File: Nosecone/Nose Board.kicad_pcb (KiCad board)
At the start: 2 copper layers, 45.7 x 63.5 mm, 48 parts, among them J1 Conn_01x02, J2 Conn_02x04_Odd_Even, J3 Conn_02x03_Odd_Even, J4 Conn_Coaxial, J5 Conn_01x02, Q1 Q_PMOS_DGS, Q2 Q_PMOS_DGS, U1 RS485_converter_ISL83488, U10 MS5803-14BA, U11 MS5803-14BA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

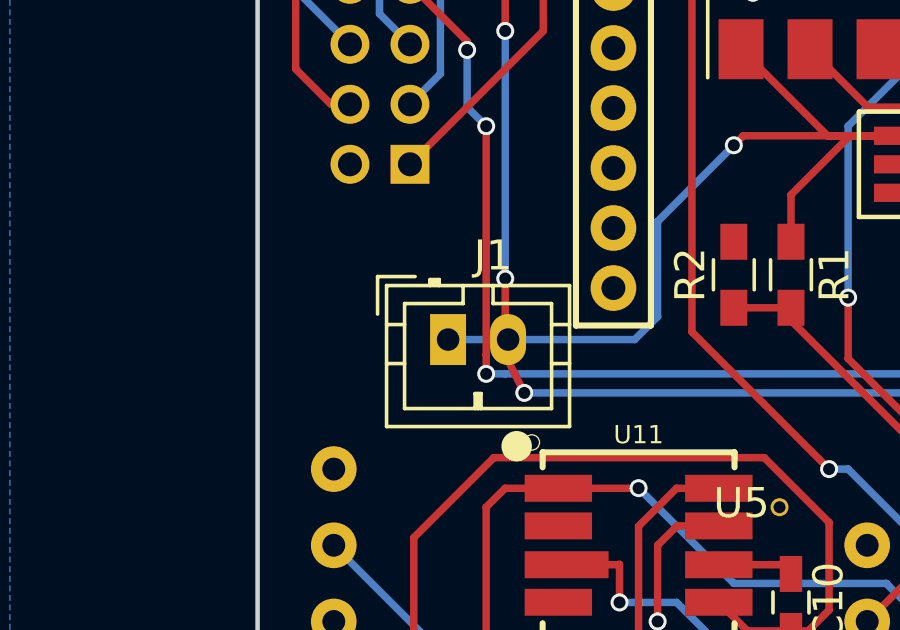
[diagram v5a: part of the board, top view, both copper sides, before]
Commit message: Layout/BoM adjustments
Known annular ring size problems, will fix those soon-ish
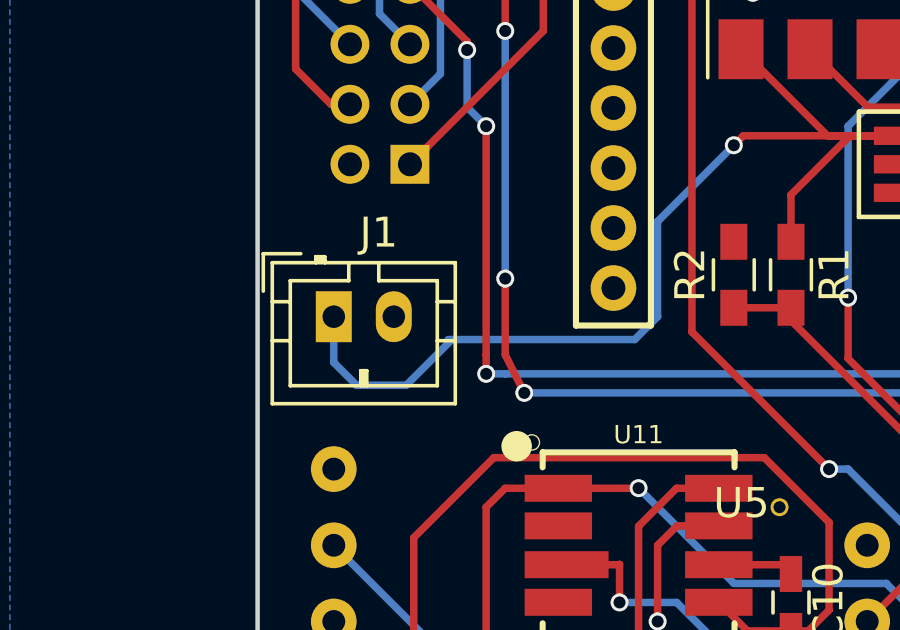
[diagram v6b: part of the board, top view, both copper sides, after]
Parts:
- moved J1 3.89 mm to (137.2, 83.8)
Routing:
- net GND: track 46.0 -> 5.07 mm, vias 4 -> 0
- net /Debug_RX: track 4.05 -> 45.0 mm, vias 1 -> 5
- net +BATT: track 31.9 -> 38.3 mm
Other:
- net class Default: via_drill 0.4 -> 0.3
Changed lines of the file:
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@@
   (general
     (links 149)
-    (no_connects 58)
-    (area 134.544999 55.804999 180.415001 119.455001)
+    (no_connects 57)
+    (area 124.46 43.18 195.580001 142.240001)
     (thickness 1.6)
-    (drawings 10)
-    (tracks 479)
+    (drawings 8)
+    (tracks 484)
     (zones 0)
     (modules 48)
@@
     (edge_width 0.15)
     (via_size 0.6)
-    (via_drill 0.4)
+    (via_drill 0.3)
     (via_min_size 0.4)
     (via_min_drill 0.3)
@@
     (visible_elements 7FFEFFFF)
     (pcbplotparams
-      (layerselection 0x00030_80000001)
+      (layerselection 0x010f0_80000001)
       (usegerberextensions false)
       (excludeedgelayer true)
       (linewidth 0.100000)
       (plotframeref false)
-      (viasonmask false)
+      (viasonmask true)
       (mode 1)
       (useauxorigin false)
@@
       (padsonsilk false)
       (subtractmaskfromsilk false)
-      (outputformat 1)
+      (outputformat 4)
       (mirror false)
-      (drillshape 1)
+      (drillshape 2)
       (scaleselection 1)
-      (outputdirectory ""))
+      (outputdirectory PDFs/))
   )
   (net 0 "")
@@
     (trace_width 0.25)
     (via_dia 0.6)
-    (via_drill 0.4)
+    (via_drill 0.3)
     (uvia_dia 0.3)
     (uvia_drill 0.1)
@@
   )
   (module Connectors_JST:JST_PH_B2B-PH-K_02x2.00mm_Straight (layer F.Cu)
-    (at 140.97 84.582)
+    (at 137.16 83.82)
     (descr "JST PH series connector, B2B-PH-K, top entry type, through hole, Datasheet: http://www.jst-mfg.com/product/pdf/eng/ePH.pdf")
     (tags "connector jst ph")
@@
   )
   (gr_circle (center 176.149 67.437) (end 177.419 68.072) (layer F.SilkS) (width 0.2))
-  (dimension 58.42 (width 0.3) (layer F.SilkS)
-    (gr_text "58.420 mm" (at 204.55 85.09 270) (layer F.SilkS)
-      (effects (font (size 1.5 1.5) (thickness 0.3)))
-    )
-    (feature1 (pts (xy 177.8 114.3) (xy 205.9 114.3)))
-    (feature2 (pts (xy 177.8 55.88) (xy 205.9 55.88)))
-    (crossbar (pts (xy 203.2 55.88) (xy 203.2 114.3)))
-    (arrow1a (pts (xy 203.2 114.3) (xy 202.613579 113.173496)))
-    (arrow1b (pts (xy 203.2 114.3) (xy 203.786421 113.173496)))
-    (arrow2a (pts (xy 203.2 55.88) (xy 202.613579 57.006504)))
-    (arrow2b (pts (xy 203.2 55.88) (xy 203.786421 57.006504)))
-  )
-  (dimension 45.72 (width 0.3) (layer F.SilkS)
-    (gr_text "45.720 mm" (at 157.48 51.99) (layer F.SilkS)
-      (effects (font (size 1.5 1.5) (thickness 0.3)))
-    )
-    (feature1 (pts (xy 180.34 58.42) (xy 180.34 50.64)))
-    (feature2 (pts (xy 134.62 58.42) (xy 134.62 50.64)))
-    (crossbar (pts (xy 134.62 53.34) (xy 180.34 53.34)))
-    (arrow1a (pts (xy 180.34 53.34) (xy 179.213496 53.926421)))
-    (arrow1b (pts (xy 180.34 53.34) (xy 179.213496 52.753579)))
-    (arrow2a (pts (xy 134.62 53.34) (xy 135.746504 53.926421)))
-    (arrow2b (pts (xy 134.62 53.34) (xy 135.746504 52.753579)))
-  )
   (gr_line (start 134.62 119.38) (end 134.62 55.88) (angle 90) (layer Edge.Cuts) (width 0.15))
   (gr_line (start 180.34 119.38) (end 134.62 119.38) (angle 90) (layer Edge.Cuts) (width 0.15))
@@
   (segment (start 173.99 100.16) (end 173.99 100.076) (width 0.25) (layer F.Cu) (net 0))
   (segment (start 168.783 110.424) (end 168.783 110.744) (width 0.25) (layer B.Cu) (net 0))
-  (segment (start 140.97 84.582) (end 147.193 84.582) (width 0.25) (layer B.Cu) (net 1))
+  (segment (start 137.16 83.82) (end 137.16 85.344) (width 0.25) (layer B.Cu) (net 1) (status 400000))
+  (segment (start 139.573 86.106) (end 141.097 84.582) (width 0.25) (layer B.Cu) (net 1))
+  (segment (start 137.922 86.106) (end 139.573 86.106) (width 0.25) (layer B.Cu) (net 1))
+  (segment (start 137.16 85.344) (end 137.922 86.106) (width 0.25) (layer B.Cu) (net 1))
+  (segment (start 140.97 84.582) (end 141.097 84.582) (width 0.25) (layer B.Cu) (net 1))
+  (segment (start 141.097 84.582) (end 147.193 84.582) (width 0.25) (layer B.Cu) (net 1))
   (segment (start 150.81 77.79) (end 155.915 77.79) (width 0.25) (layer F.Cu) (net 1))
   (segment (start 150.495 78.105) (end 150.81 77.79) (width 0.25) (layer F.Cu) (net 1))
@@
   (segment (start 152.4 92.395) (end 152.0927 92.0877) (width 0.25) (layer F.Cu) (net 2))
   (segment (start 152.0927 92.0877) (end 149.99462 92.0877) (width 0.25) (layer F.Cu) (net 2))
-  (segment (start 142.875 85.09) (end 143.51 86.36) (width 0.25) (layer F.Cu) (net 2))
-  (segment (start 142.875 82.55) (end 142.875 85.09) (width 0.25) (layer F.Cu) (net 2))
-  (via (at 142.875 82.55) (size 0.6) (drill 0.4) (layers F.Cu B.Cu) (net 2))
-  (segment (start 142.875 82.55) (end 142.875 82.55) (width 0.25) (layer B.Cu) (net 2))
-  (segment (start 142.875 74.295) (end 142.875 82.55) (width 0.25) (layer B.Cu) (net 2))
-  (via (at 142.875 74.295) (size 0.6) (drill 0.4) (layers F.Cu B.Cu) (net 2))
-  (segment (start 142.875 71.12) (end 142.875 74.295) (width 0.25) (layer F.Cu) (net 2))
-  (segment (start 141.605 69.85) (end 142.875 71.12) (width 0.25) (layer F.Cu) (net 2))
-  (segment (start 138.43 69.85) (end 141.605 69.85) (width 0.25) (layer F.Cu) (net 2))
-  (via (at 143.51 86.36) (size 0.6) (drill 0.4) (layers F.Cu B.Cu) (net 2))
-  (segment (start 137.7 70.58) (end 138.43 69.85) (width 0.25) (layer F.Cu) (net 2))
-  (segment (start 143.51 86.36) (end 158.115 86.36) (width 0.25) (layer B.Cu) (net 2))
-  (via (at 158.115 86.36) (size 0.6) (drill 0.4) (layers F.Cu B.Cu) (net 2))
-  (segment (start 158.115 86.36) (end 163.068 86.106) (width 0.25) (layer F.Cu) (net 2))
   (segment (start 144.145 60.735) (end 144.145 62.865) (width 0.25) (layer B.Cu) (net 3))
   (segment (start 140.716 75.724) (end 139.7 76.74) (width 0.25) (layer B.Cu) (net 3))
@@
   (via (at 163.83 85.09) (size 0.6) (drill 0.4) (layers F.Cu B.Cu) (net 43))
   (segment (start 164.3 85.56) (end 163.83 85.09) (width 0.25) (layer B.Cu) (net 43))
+  (segment (start 142.875 85.09) (end 143.51 86.36) (width 0.25) (layer F.Cu) (net 44))
+  (segment (start 142.875 82.55) (end 142.875 85.09) (width 0.25) (layer F.Cu) (net 44))
+  (via (at 142.875 82.55) (size 0.6) (drill 0.4) (layers F.Cu B.Cu) (net 44))
+  (segment (start 142.875 82.55) (end 142.875 82.55) (width 0.25) (layer B.Cu) (net 44))
+  (segment (start 142.875 74.295) (end 142.875 82.55) (width 0.25) (layer B.Cu) (net 44))
+  (via (at 142.875 74.295) (size 0.6) (drill 0.4) (layers F.Cu B.Cu) (net 44))
+  (segment (start 142.875 71.12) (end 142.875 74.295) (width 0.25) (layer F.Cu) (net 44))
+  (segment (start 141.605 69.85) (end 142.875 71.12) (width 0.25) (layer F.Cu) (net 44))
+  (segment (start 138.43 69.85) (end 141.605 69.85) (width 0.25) (layer F.Cu) (net 44))
+  (via (at 143.51 86.36) (size 0.6) (drill 0.4) (layers F.Cu B.Cu) (net 44))
+  (segment (start 137.7 70.58) (end 138.43 69.85) (width 0.25) (layer F.Cu) (net 44))
+  (segment (start 143.51 86.36) (end 158.115 86.36) (width 0.25) (layer B.Cu) (net 44))
+  (via (at 158.115 86.36) (size 0.6) (drill 0.4) (layers F.Cu B.Cu) (net 44))
+  (segment (start 158.115 86.36) (end 163.068 86.106) (width 0.25) (layer F.Cu) (net 44))
+  (via (at 163.068 86.106) (size 0.6) (drill 0.4) (layers F.Cu B.Cu) (net 44))
   (segment (start 137.7 72.74) (end 137.7 70.58) (width 0.25) (layer F.Cu) (net 44))
   (segment (start 163.5 86.03) (end 163.5 87.48) (width 0.25) (layer B.Cu) (net 44))
   (segment (start 163.068 86.106) (end 163.5 86.03) (width 0.25) (layer B.Cu) (net 44))
-  (via (at 163.068 86.106) (size 0.6) (drill 0.4) (layers F.Cu B.Cu) (net 44))
   (segment (start 165.9 87.48) (end 165.9 94.069) (width 0.25) (layer B.Cu) (net 45))
   (segment (start 155.194 111.76) (end 153.67 111.76) (width 0.25) (layer B.Cu) (net 45))
